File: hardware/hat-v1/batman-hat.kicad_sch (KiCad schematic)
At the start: 0 parts

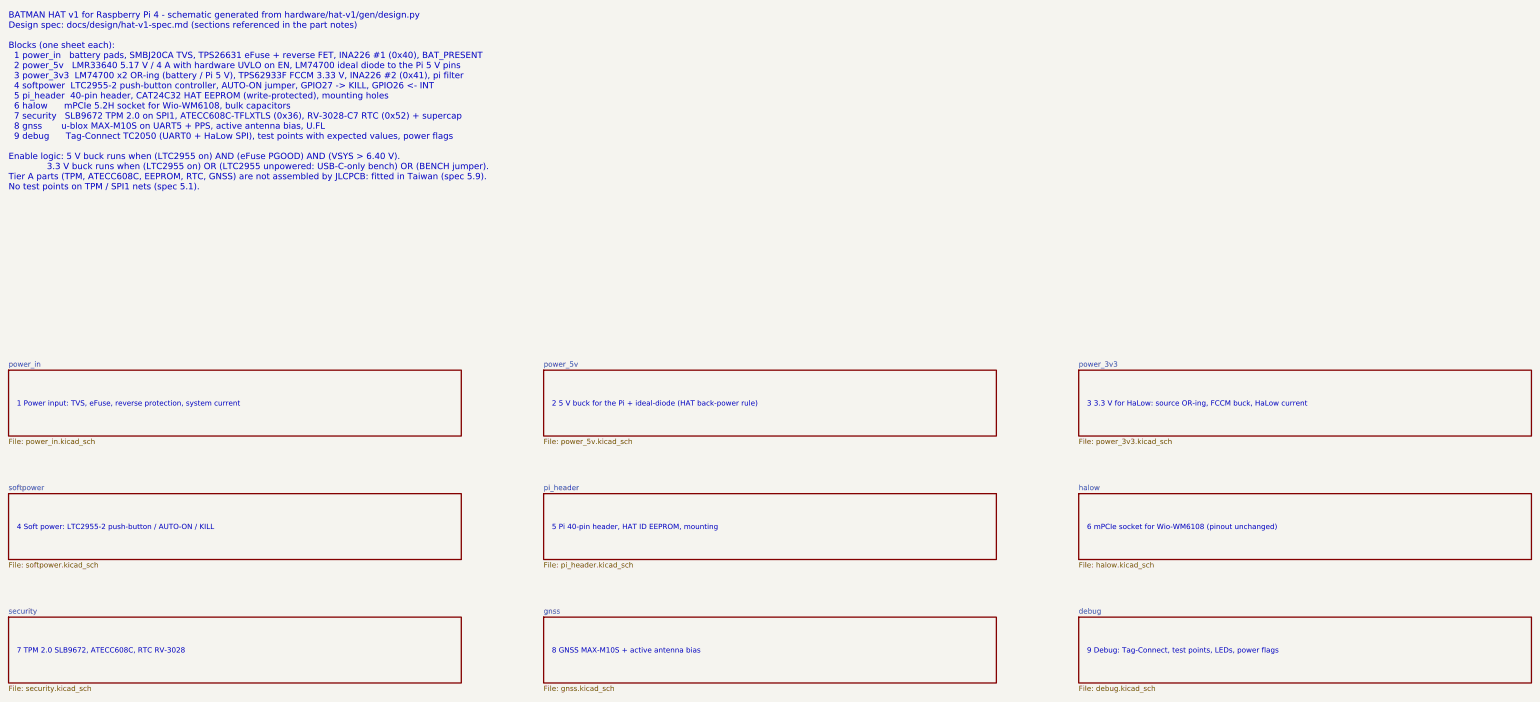
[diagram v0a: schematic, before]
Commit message: HAT v1: option D power tree - HaLow 3.3 V buck fed from the Pi 5 V rail
- TPS62933F input moved from the OR node to 5V_PI (HAT 5 V buck or Pi USB-C),
  as on the WM1302 HAT: the HaLow card still runs on USB-C only
- EN pulled up to the Pi 3.3 V through 100k: no back-feed into an unpowered Pi,
  HAT+ STANDBY turns the card off; LTC2955 off already removes 5 V
- removed: LM74700 x2 + FET x2 + VCAP x2 (OR-ing), BENCH jumper + Q9/R24, Q8,
  HAT ID EEPROM + WP jumper + pull-ups + decoupling, OR_NODE test point
- kept the battery-present divider (spec review #22)
- checker: HaLow EN set points; spec 5.5.5 power tree review; re-placed board

Co-Authored-By: Claude Opus 5.5 <noreply@anthropic.com>
Claude-Session: https://claude.ai/code/session_01MLRuxTEmuMV82xcNLE62jW
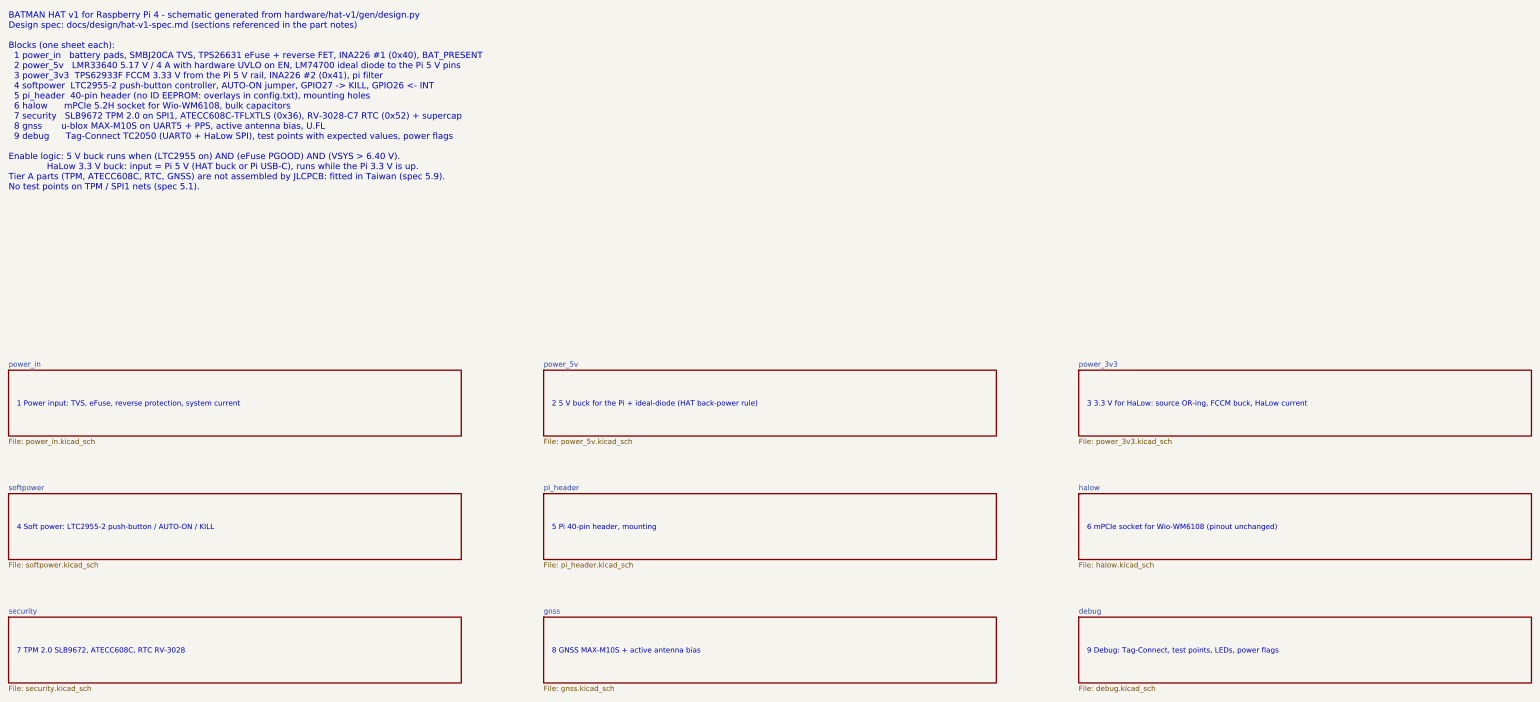
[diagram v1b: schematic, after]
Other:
- note added: "5 Pi 40-pin header, mounting"
- note removed: "5 Pi 40-pin header, HAT ID EEPROM, mounting"
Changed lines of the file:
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@@
     (instances (project "batman-hat" (path "/bad0bf22-4662-5834-886f-55d01014b15a" (page "6"))))
   )
-  (text "5 Pi 40-pin header, HAT ID EEPROM, mounting" (at 147 149 0) (effects (font (size 1.27 1.27)) (justify left bottom)))
+  (text "5 Pi 40-pin header, mounting" (at 147 149 0) (effects (font (size 1.27 1.27)) (justify left bottom)))
   (sheet (at 275 140) (size 110 16) (fields_autoplaced) (stroke (width 0.1524) (type solid)) (fill (color 0 0 0 0.0000))
     (property "Sheetname" "halow" (at 275 139.3 0) (effects (font (size 1.27 1.27)) (justify left bottom)))
@@
   )
   (text "9 Debug: Tag-Connect, test points, LEDs, power flags" (at 277 179 0) (effects (font (size 1.27 1.27)) (justify left bottom)))
-  (text "BATMAN HAT v1 for Raspberry Pi 4 - schematic generated from hardware/hat-v1/gen/design.py\nDesign spec: docs/design/hat-v1-spec.md (sections referenced in the part notes)\n\nBlocks (one sheet each):\n  1 power_in   battery pads, SMBJ20CA TVS, TPS26631 eFuse + reverse FET, INA226 #1 (0x40), BAT_PRESENT\n  2 power_5v   LMR33640 5.17 V / 4 A with hardware UVLO on EN, LM74700 ideal diode to the Pi 5 V pins\n  3 power_3v3  LM74700 x2 OR-ing (battery / Pi 5 V), TPS62933F FCCM 3.33 V, INA226 #2 (0x41), pi filter\n  4 softpower  LTC2955-2 push-button controller, AUTO-ON jumper, GPIO27 -> KILL, GPIO26 <- INT\n  5 pi_header  40-pin header, CAT24C32 HAT EEPROM (write-protected), mounting holes\n  6 halow      mPCIe 5.2H socket for Wio-WM6108, bulk capacitors\n  7 security   SLB9672 TPM 2.0 on SPI1, ATECC608C-TFLXTLS (0x36), RV-3028-C7 RTC (0x52) + supercap\n  8 gnss       u-blox MAX-M10S on UART5 + PPS, active antenna bias, U.FL\n  9 debug      Tag-Connect TC2050 (UART0 + HaLow SPI), test points with expected values, power flags\n\nEnable logic: 5 V buck runs when (LTC2955 on) AND (eFuse PGOOD) AND (VSYS > 6.40 V).\n              3.3 V buck runs when (LTC2955 on) OR (LTC2955 unpowered: USB-C-only bench) OR (BENCH jumper).\nTier A parts (TPM, ATECC608C, EEPROM, RTC, GNSS) are not assembled by JLCPCB: fitted in Taiwan (spec 5.9).\nNo test points on TPM / SPI1 nets (spec 5.1)." (at 15 23 0) (effects (font (size 1.524 1.524)) (justify left top)))
+  (text "BATMAN HAT v1 for Raspberry Pi 4 - schematic generated from hardware/hat-v1/gen/design.py\nDesign spec: docs/design/hat-v1-spec.md (sections referenced in the part notes)\n\nBlocks (one sheet each):\n  1 power_in   battery pads, SMBJ20CA TVS, TPS26631 eFuse + reverse FET, INA226 #1 (0x40), BAT_PRESENT\n  2 power_5v   LMR33640 5.17 V / 4 A with hardware UVLO on EN, LM74700 ideal diode to the Pi 5 V pins\n  3 power_3v3  TPS62933F FCCM 3.33 V from the Pi 5 V rail, INA226 #2 (0x41), pi filter\n  4 softpower  LTC2955-2 push-button controller, AUTO-ON jumper, GPIO27 -> KILL, GPIO26 <- INT\n  5 pi_header  40-pin header (no ID EEPROM: overlays in config.txt), mounting holes\n  6 halow      mPCIe 5.2H socket for Wio-WM6108, bulk capacitors\n  7 security   SLB9672 TPM 2.0 on SPI1, ATECC608C-TFLXTLS (0x36), RV-3028-C7 RTC (0x52) + supercap\n  8 gnss       u-blox MAX-M10S on UART5 + PPS, active antenna bias, U.FL\n  9 debug      Tag-Connect TC2050 (UART0 + HaLow SPI), test points with expected values, power flags\n\nEnable logic: 5 V buck runs when (LTC2955 on) AND (eFuse PGOOD) AND (VSYS > 6.40 V).\n              HaLow 3.3 V buck: input = Pi 5 V (HAT buck or Pi USB-C), runs while the Pi 3.3 V is up.\nTier A parts (TPM, ATECC608C, RTC, GNSS) are not assembled by JLCPCB: fitted in Taiwan (spec 5.9).\nNo test points on TPM / SPI1 nets (spec 5.1)." (at 15 23 0) (effects (font (size 1.524 1.524)) (justify left top)))
   (sheet_instances (path "/" (page "1")))
 )
